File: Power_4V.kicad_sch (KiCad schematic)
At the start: 9 parts, among them U6 AP63200WU

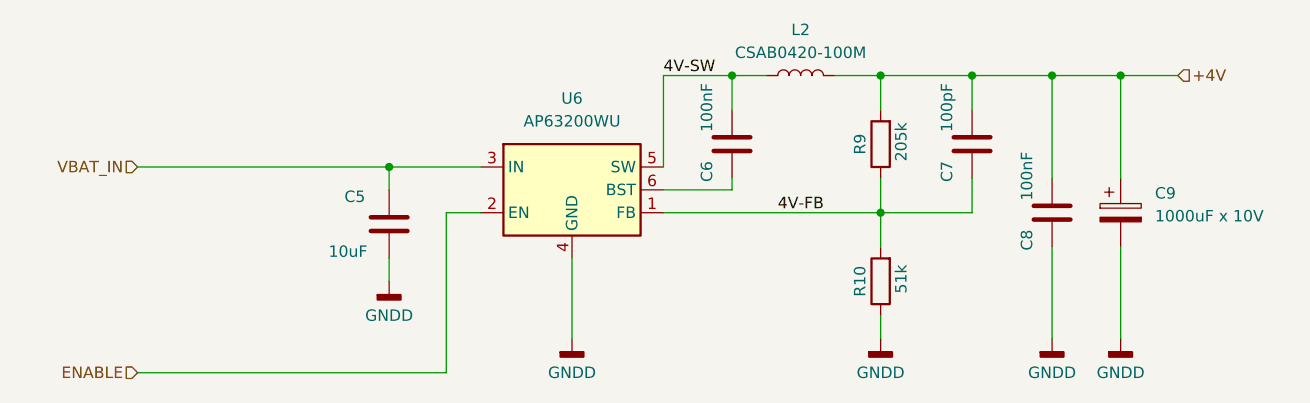
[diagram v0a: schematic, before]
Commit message: Replace SIM800C-DS with A7682E
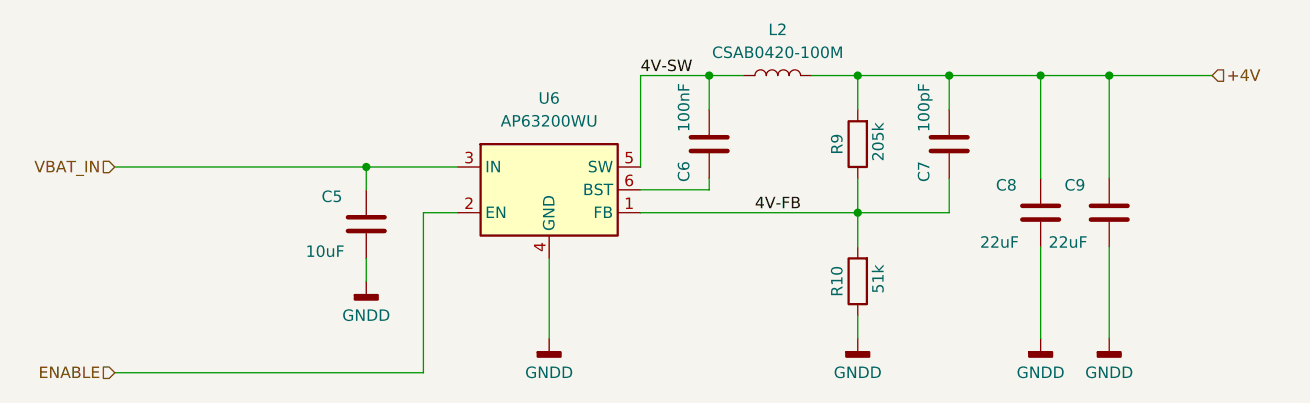
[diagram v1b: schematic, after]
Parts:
- removed C9: 1000uF x 10V, Capacitor_SMD:CP_Elec_10x10.5, symbol Device:C_Polarized
- added C9: 22uF, Capacitor_SMD:C_0805_2012Metric_Pad1.18x1.45mm_HandSolder, symbol Device:C
- C8: value 100nF -> 22uF; MPN CC0805KRX7R8BB104 -> CC0805MKX5R8BB226
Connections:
- net +4V: now also C9.2
- net GNDD: now also C9.1

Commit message: USB connector inversion fix
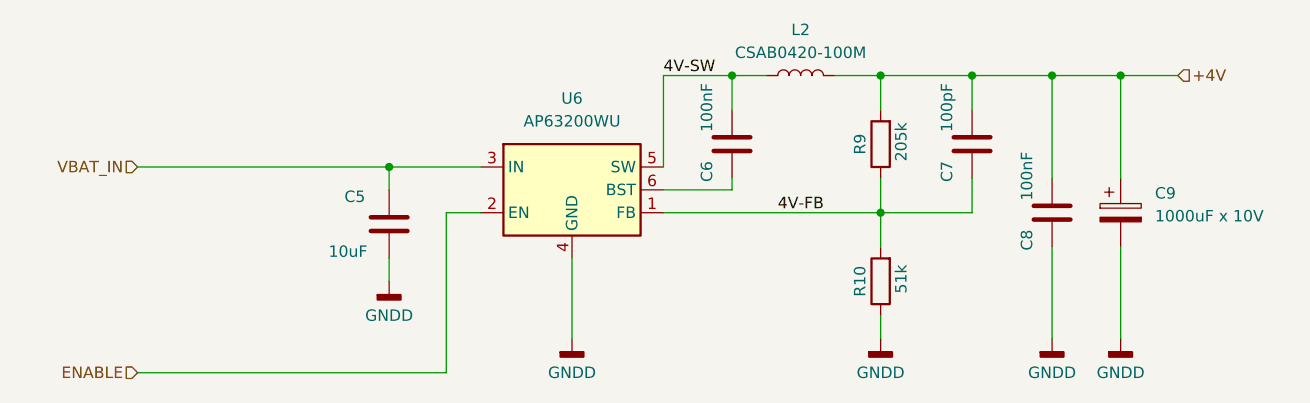
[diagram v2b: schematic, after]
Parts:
- removed C9: 22uF, Capacitor_SMD:C_0805_2012Metric_Pad1.18x1.45mm_HandSolder, symbol Device:C
- added C9: 1000uF x 10V, Capacitor_SMD:CP_Elec_10x10.5, symbol Device:C_Polarized
- C8: value 22uF -> 100nF; MPN CC0805MKX5R8BB226 -> CC0805KRX7R8BB104
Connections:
- net +4V: now also C9.1
- net GNDD: now also C9.2
